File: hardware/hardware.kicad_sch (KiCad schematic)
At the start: 38 parts, among them J1 USB_A, J2 BOOT, J3 SWD, J4 USR_LEFT, J5 USR_RIGHT, J6 Conn_01x04, SW1 SW_Push, U1 MCP2551-I_SN, U2 LM317_SOT-223-3.3V, U3 STM32F107RBTx, U4 TJA1020, Y1 Crystal

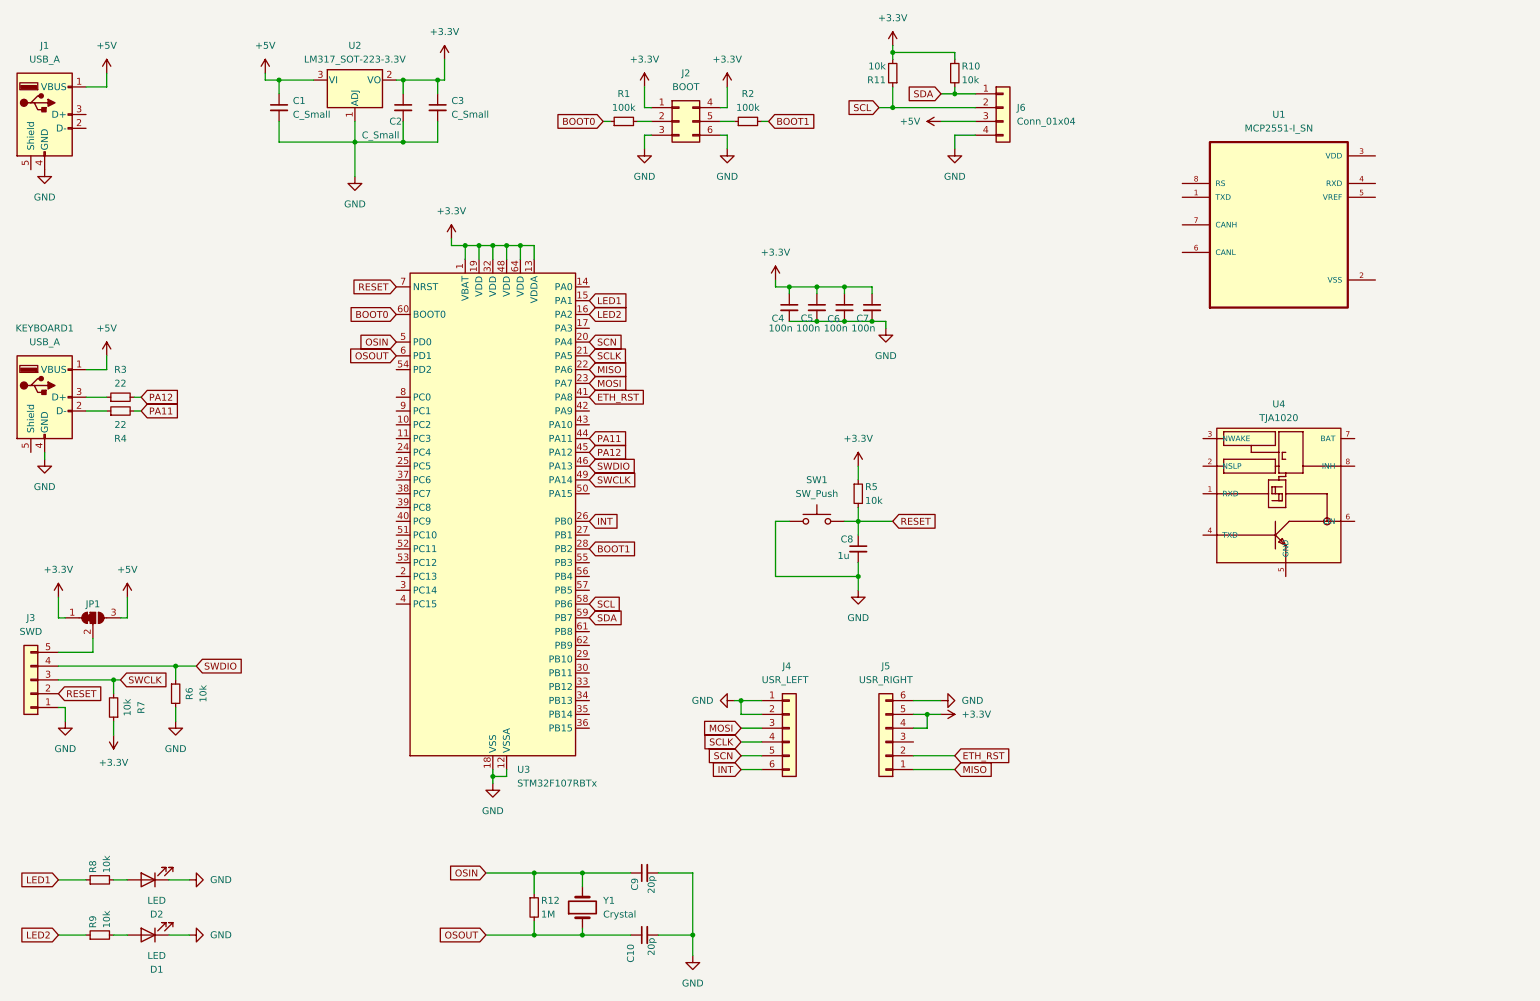
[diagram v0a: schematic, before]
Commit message: add lin control bus
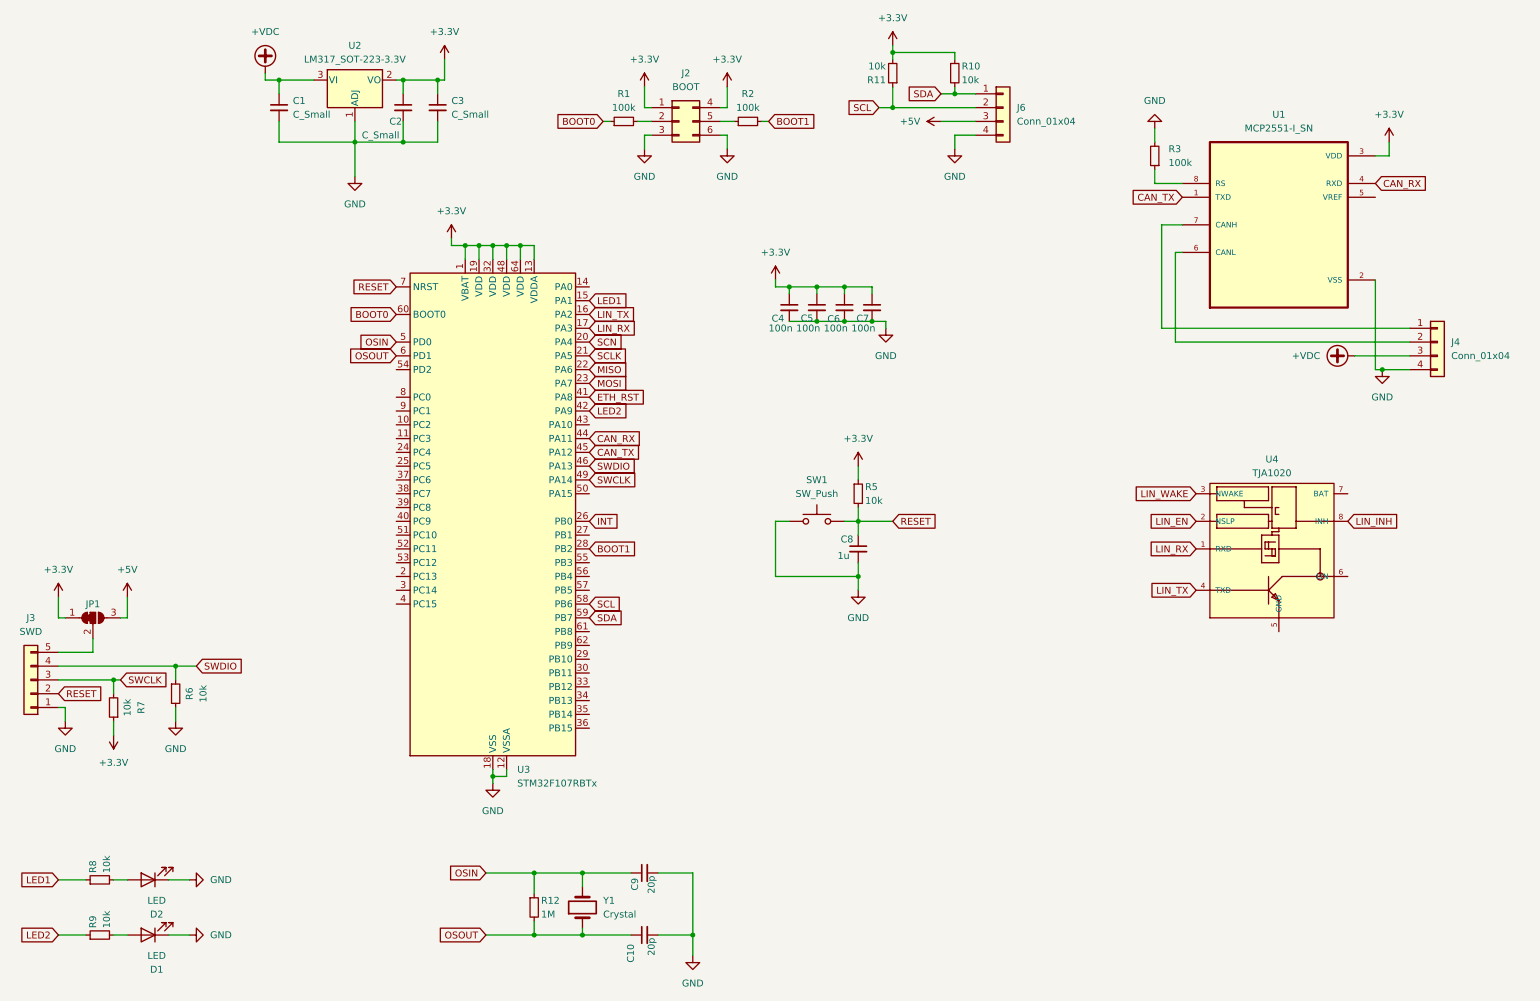
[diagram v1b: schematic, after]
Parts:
- removed J1: USB_A, Connector_USB:USB_Micro-B_Molex-105017-0001, symbol Connector:USB_A
- removed J4: USR_LEFT, Connector_PinHeader_2.54mm:PinHeader_1x06_P2.54mm_Vertical, symbol Connector_Generic:Conn_01x06
- removed J5: USR_RIGHT, Connector_PinHeader_2.54mm:PinHeader_1x06_P2.54mm_Vertical, symbol Connector_Generic:Conn_01x06
- removed KEYBOARD1: USB_A, Connector_USB:USB_A_TE_292303-7_Horizontal, symbol Connector:USB_A
- removed R4: 22, Resistor_SMD:R_0603_1608Metric, symbol Device:R_Small
- added J4: Conn_01x04, symbol Connector_Generic:Conn_01x04
- R3: value 22 -> 100k
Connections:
- net PA11 is gone; now on net CAN_RX: U3.44 (PA11)
- net +3.3V: now also U1.3 (VDD)
- net +5V: no longer C1.1, U2.3 (VI)
- net GND: now also R3.2, U1.2 (VSS), J4.4 (Pin_4)
- net LED2: now also U3.42 (PA9); no longer U3.16 (PA2)
- net LIN_RX: now reaches U3.17 (PA3)
- net LIN_RX: now also U4.1 (RXD)
- net at R3.1: now also U1.8 (RS)
- net LIN_EN: now reaches U4.2 (NSLP)
- net LIN_WAKE: now reaches U4.3 (NWAKE)
- net LIN_TX: now reaches U4.4 (TXD)
- net LIN_TX: now also U3.16 (PA2)
- net LIN_INH: now reaches U4.8 (INH)
- net CAN_TX: now reaches U1.1 (TXD)
- net CAN_TX: now also U3.45 (PA12)
- net CAN_RX: now reaches U1.4 (RXD)
- net at U1.6 (CANL): now also J4.2 (Pin_2)
- net at U1.7 (CANH): now also J4.1 (Pin_1)
- removed net PA12: R3.2, U3.45 (PA12)
- new net +VDC: C1.1, J4.3 (Pin_3), U2.3 (VI)
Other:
- moved on the sheet: U4

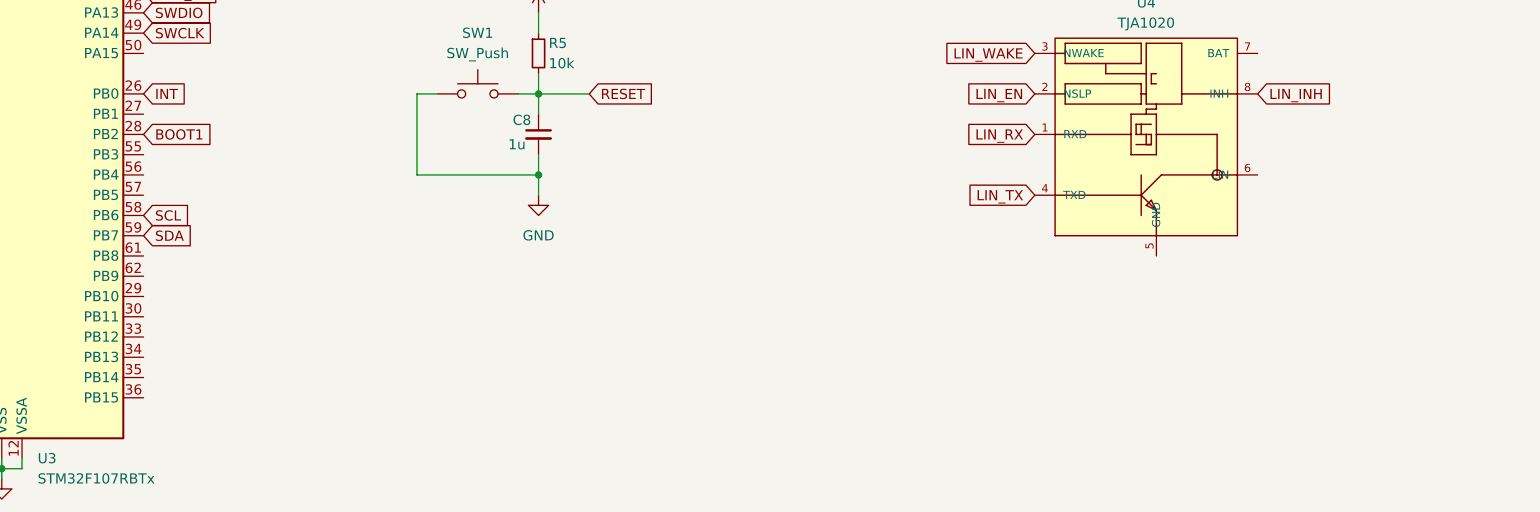
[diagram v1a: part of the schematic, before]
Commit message: add lin + can connectors
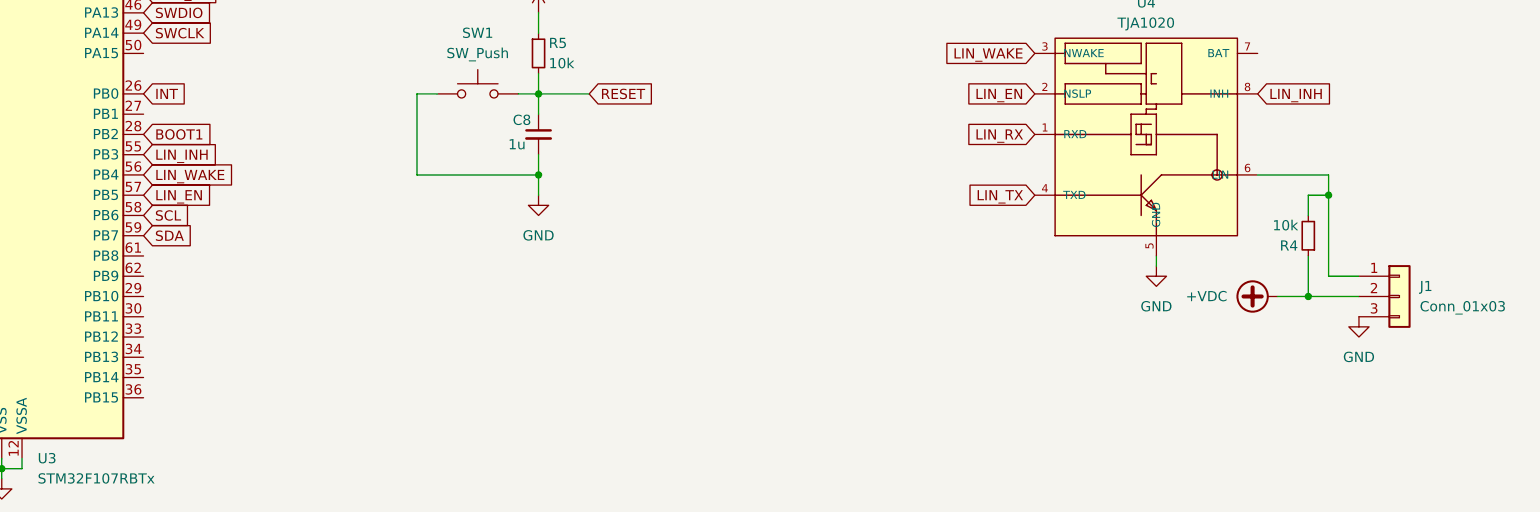
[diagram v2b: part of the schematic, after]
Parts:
- added J1: Conn_01x03, Connector_Phoenix_MC:PhoenixContact_MCV_1,5_3-GF-3.5_1x03_P3.50mm_Vertical_ThreadedFlange, symbol Connector_Generic:Conn_01x03
- added R4: 10k, Resistor_SMD:R_0603_1608Metric, symbol Device:R_Small
- J4: footprint (none) -> Connector_Phoenix_MC:PhoenixContact_MCV_1,5_4-GF-3.5_1x04_P3.50mm_Vertical_ThreadedFlange_MountHole
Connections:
- net +VDC: now also J1.2 (Pin_2), R4.1
- net GND: now also U4.5 (GND), J1.3 (Pin_3)
- net LIN_EN: now also U3.57 (PB5)
- net LIN_INH: now also U3.55 (PB3)
- net LIN_WAKE: now also U3.56 (PB4)
- net at U4.6 (LIN): now also J1.1 (Pin_1), R4.2

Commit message: upgrade lin footprint
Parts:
- J1: footprint Connector_Phoenix_MC:PhoenixContact_MCV_1,5_3-GF-3.5_1x03_P3.50mm_Vertical_ThreadedFlange -> Connector_Phoenix_MC:PhoenixContact_MCV_1,5_3-GF-3.5_1x03_P3.50mm_Vertical_ThreadedFlange_MountHole
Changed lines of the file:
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@@
 			)
 		)
-		(property "Footprint" "Connector_Phoenix_MC:PhoenixContact_MCV_1,5_3-GF-3.5_1x03_P3.50mm_Vertical_ThreadedFlange"
+		(property "Footprint" "Connector_Phoenix_MC:PhoenixContact_MCV_1,5_3-GF-3.5_1x03_P3.50mm_Vertical_ThreadedFlange_MountHole"
 			(at 281.94 130.81 0)
 			(effects

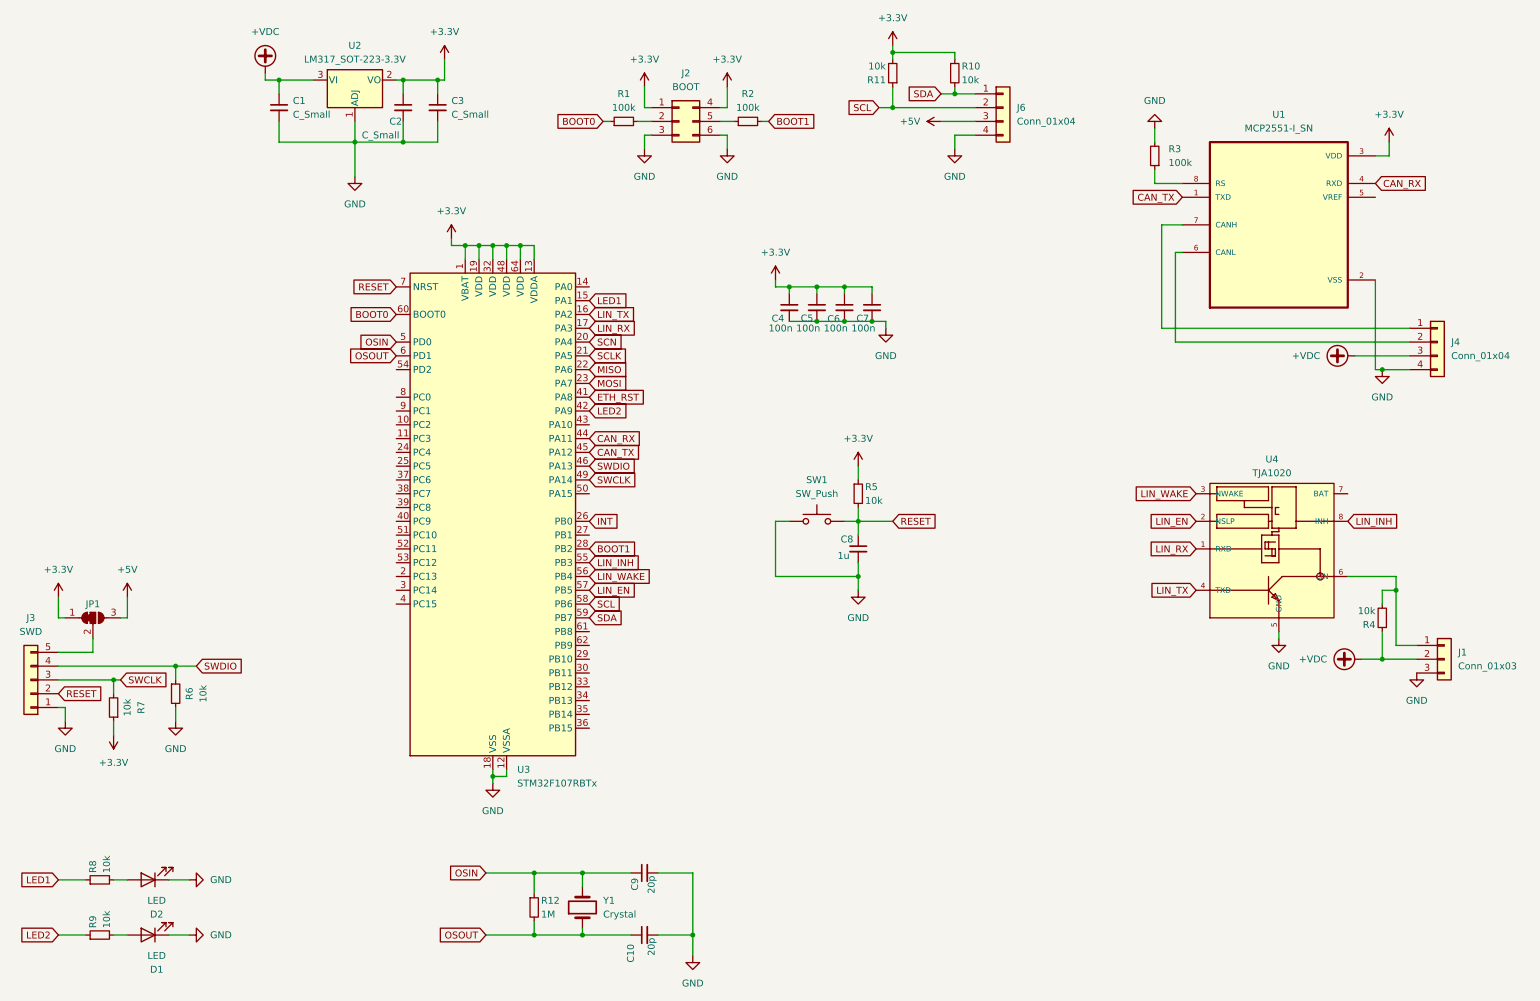
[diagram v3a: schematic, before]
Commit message: fix boot 0 & boot 1 pin
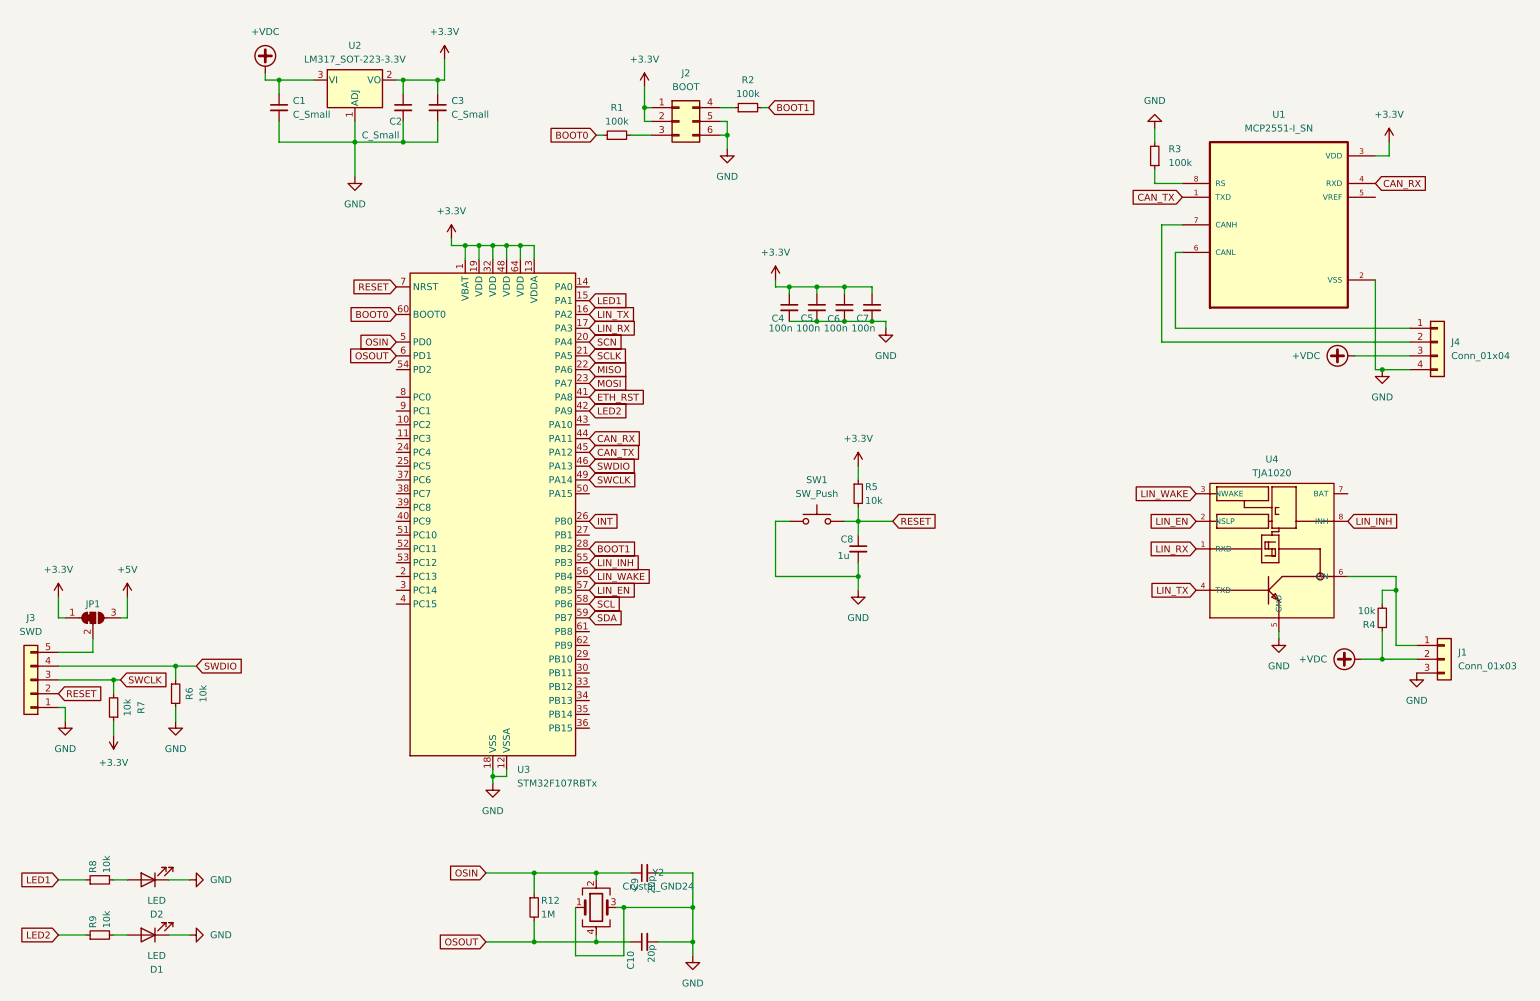
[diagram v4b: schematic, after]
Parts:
- removed J6: Conn_01x04, Connector_PinHeader_2.54mm:PinHeader_1x04_P2.54mm_Vertical, symbol Connector_Generic:Conn_01x04
- removed R10, R11: 10k, Resistor_SMD:R_0603_1608Metric, symbol Device:R_Small
- removed Y1: Crystal, Crystal:Crystal_SMD_HC49-SD, symbol Device:Crystal
- added Y2: Crystal_GND24, Crystal:Crystal_SMD_3225-4Pin_3.2x2.5mm, symbol Device:Crystal_GND24
- J2: footprint Library:PinHeader_2x03_P2.54mm_Vertical_new -> Connector_PinHeader_2.54mm:PinHeader_2x03_P2.54mm_Vertical_SMD
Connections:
- net +3.3V: now also J2.2 (Pin_2); no longer J2.4 (Pin_4)
- net GND: now also J2.5 (Pin_5), Y2.1, Y2.3; no longer J2.3 (Pin_3)
- net OSIN: now also Y2.2
- net OSOUT: now also Y2.4
- net at J4.1 (Pin_1): now also U1.6 (CANL); no longer U1.7 (CANH)
- net at J4.2 (Pin_2): now also U1.7 (CANH); no longer U1.6 (CANL)
- net at R2.1: now also J2.4 (Pin_4); no longer J2.5 (Pin_5)
- net at R1.2: now also J2.3 (Pin_3); no longer J2.2 (Pin_2)
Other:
- moved on the sheet: C10, R1, R2
